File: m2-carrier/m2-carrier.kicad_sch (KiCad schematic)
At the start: 29 parts, among them P1 ESC1_VCC, P2 ESC1_GND, P3 LIPO_VCC, P4 LIPO_GND, P5 ESC2_VCC, P6 ESC2_GND, Q1 DMP3013SFV, U2 LD1117S33TR_SOT223, U6 LMR16030SDDAR

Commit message: new stuff
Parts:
- removed C21, C23: 2.2uF, Capacitor_SMD:C_0402_1005Metric, symbol Device:C_Small
- removed C24, C27: 47uF, Capacitor_SMD:C_0402_1005Metric, symbol Device:C_Small
- removed C28, C29, C32: 100nF, Capacitor_SMD:C_0402_1005Metric, symbol Device:C_Small
- removed C3, C5: 10uF, Capacitor_SMD:C_0402_1005Metric_Pad0.74x0.62mm_HandSolder, symbol Device:C_Small
- removed C30: 10uF, Capacitor_SMD:C_0402_1005Metric, symbol Device:C_Small
- removed C31: C_SS, Capacitor_SMD:C_0402_1005Metric, symbol Device:C_Small
- removed D7: B340AG, Diode_SMD:D_SMB, symbol Device:D_Schottky_Small
- removed D8: MMBZ5242B, Diode_SMD:D_SOT-23_ANK, symbol Diode:BZV55C12
- removed JP1: SolderJumper_3_Open, Jumper:SolderJumper-3_P1.3mm_Open_RoundedPad1.0x1.5mm_NumberLabels, symbol Jumper:SolderJumper_3_Open
- removed JP3: IO_EN, Jumper:SolderJumper-2_P1.3mm_Open_RoundedPad1.0x1.5mm, symbol Jumper:SolderJumper_2_Open
- removed L2: 8.2uH, Inductor_SMD:L_Bourns_SRP7028A_7.3x6.6mm, symbol Device:L_Small
- removed P1: ESC1_VCC, TestPoint:TestPoint_Pad_2.0x2.0mm, symbol hermes_v1-rescue:PAD_SMD-pkl_misc
- removed P2: ESC1_GND, TestPoint:TestPoint_Pad_D2.0mm, symbol hermes_v1-rescue:PAD_SMD-pkl_misc
- removed P3: LIPO_VCC, TestPoint:TestPoint_Pad_2.0x2.0mm, symbol hermes_v1-rescue:PAD_SMD-pkl_misc
- removed P4: LIPO_GND, TestPoint:TestPoint_Pad_D2.0mm, symbol hermes_v1-rescue:PAD_SMD-pkl_misc
- removed P5: ESC2_VCC, TestPoint:TestPoint_Pad_2.0x2.0mm, symbol hermes_v1-rescue:PAD_SMD-pkl_misc
- removed P6: ESC2_GND, TestPoint:TestPoint_Pad_D2.0mm, symbol hermes_v1-rescue:PAD_SMD-pkl_misc
- removed Q1: DMP3013SFV, Package_SON:Diodes_PowerDI3333-8, symbol Transistor_FET:DMP3013SFV
- removed R10: 49.9K, Resistor_SMD:R_0402_1005Metric, symbol Device:R_Small
- removed R11: 17.8K, Resistor_SMD:R_0402_1005Metric, symbol Device:R_Small
- removed R17: 12K, Resistor_SMD:R_0402_1005Metric, symbol Device:R_Small
- removed R8: 100K, Resistor_SMD:R_0402_1005Metric, symbol Device:R_Small
- removed U2: LD1117S33TR_SOT223, Package_TO_SOT_SMD:SOT-223-3_TabPin2, symbol Regulator_Linear:LD1117S33TR_SOT223
- removed U6: LMR16030SDDAR, Package_SO:Texas_HSOP-8-1EP_3.9x4.9mm_P1.27mm_ThermalVias, symbol Regulator_Switching:LMR33630ADDA
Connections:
- no-connect marks 1 -> 0
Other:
- removed sheet PADS
- note removed: "+5V @ 3A DC-DC Converter (4.3v-60v Input)"
- note removed: "2.1mm Tip +12v input Voltage"
- note removed: "3A RMS Current 6A I_Saturation"
- note removed: "By default, the usb port are connected to the 3.3V LDO If bridged, LDO receives power from buck regulator"
- note removed: "C_BOOT"
- note removed: "C_SS"
- note removed: "Diode to prevent reverse polarity at input"
- note removed: "ESC Solder Pads"
- note removed: "LiPo Battery Solder Pads"
- note removed: "Linear Dropout Regulator - LD1117 - 3.3V 1A"
- note removed: "Maximum input voltage: 26V"
- note removed: "Power"
- note removed: "R_FBB"
- note removed: "R_FBT"
- note removed: "Rated for 16V"
- note removed: "SOT23-3 225mW-300mW"
- note removed: "Solder-Jumper for USB_VBUS and 5V"

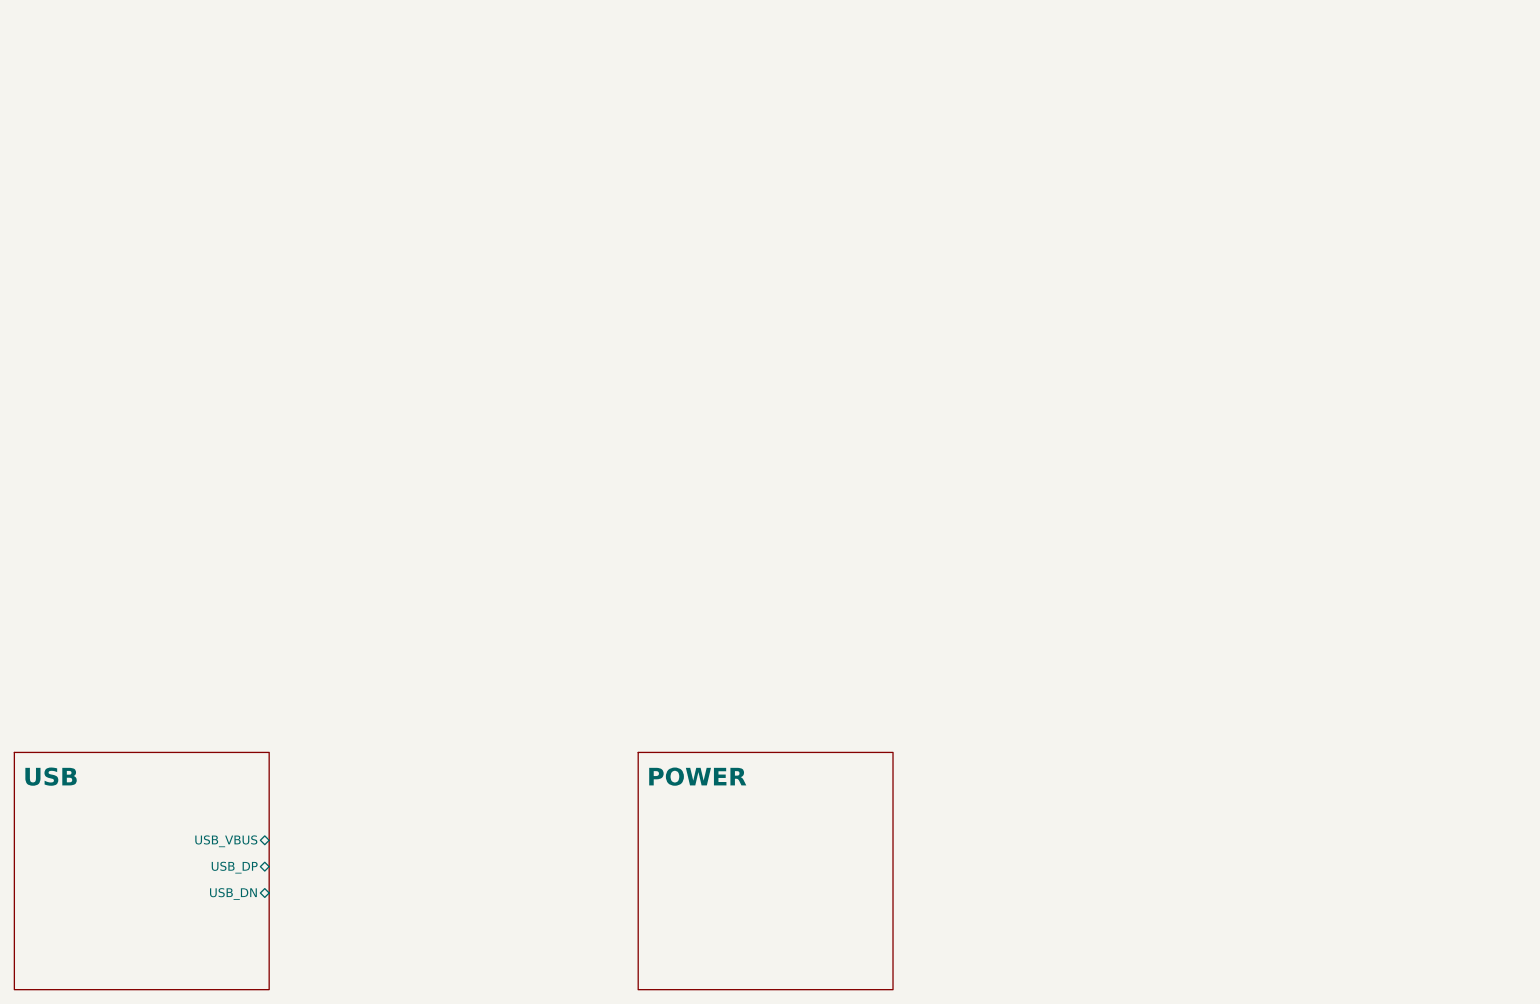
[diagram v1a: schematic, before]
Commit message: added video IC
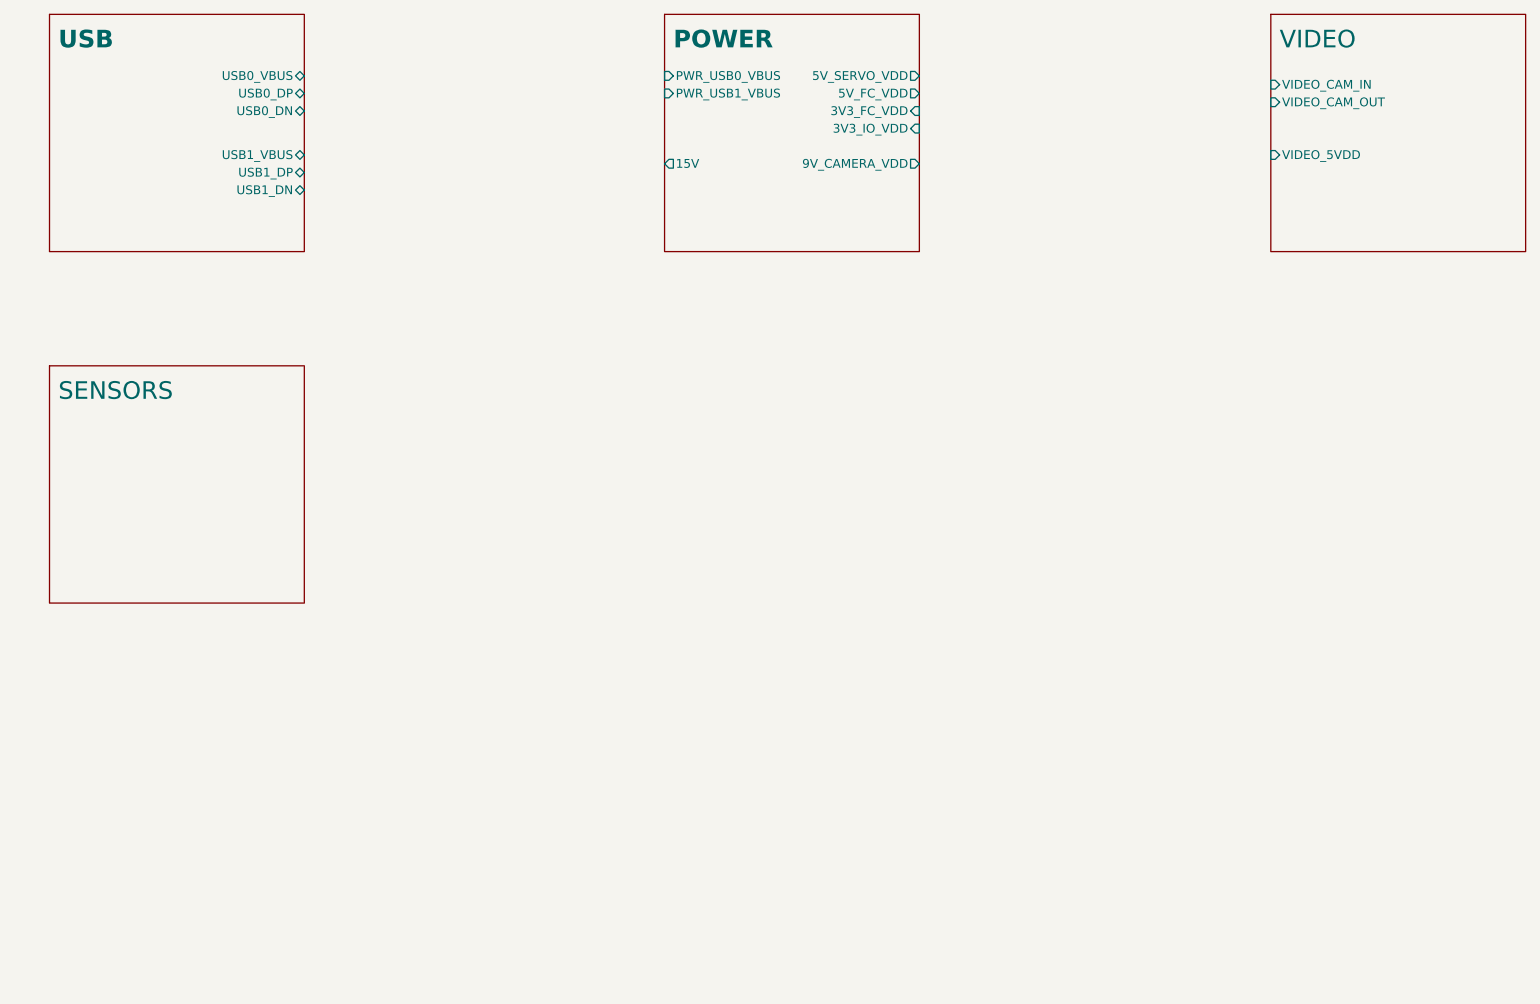
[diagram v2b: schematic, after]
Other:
- added sheet SENSORS (SENSORS.kicad_sch)
- added sheet VIDEO (VIDEO.kicad_sch)
- sheet POWER ports: added 15V, 3V3_FC_VDD, 3V3_IO_VDD, 5V_FC_VDD, 5V_SERVO_VDD, 9V_CAMERA_VDD, PWR_USB0_VBUS, PWR_USB1_VBUS; removed none
- sheet USB ports: added USB0_DN, USB0_DP, USB0_VBUS, USB1_DN, USB1_DP, USB1_VBUS; removed USB_DN, USB_DP, USB_VBUS
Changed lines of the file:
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@@
 (kicad_sch (version 20230121) (generator eeschema)
   (paper "A4")
-  (sheet (at 27.94 142.24) (size 36.83 34.29)
+  (sheet (at 209.55 35.56) (size 36.83 34.29)
+    (stroke (width 0.1524) (type solid))
+    (fill (color 194 194 194 1.0000))
+    (property "Sheetname" "VIDEO" (at 210.82 40.64 0)
+      (effects (font (face "Fira Code Retina") (size 2.54 2.54)) (justify left bottom))
+    )
+    (property "Sheetfile" "VIDEO.kicad_sch" (at 209.55 67.8946 0)
+      (effects (font (size 1.27 1.27)) (justify left top) hide)
+    )
+    (pin "VIDEO_CAM_IN" input (at 209.55 45.72 180)
+      (effects (font (size 1.27 1.27)) (justify left))
+    )
+    (pin "VIDEO_CAM_OUT" input (at 209.55 48.26 180)
+      (effects (font (size 1.27 1.27)) (justify left))
+    )
+    (pin "VIDEO_5VDD" input (at 209.55 55.88 180)
+      (effects (font (size 1.27 1.27)) (justify left))
+    )
+    (instances
+      (project "m2-carrier"
+        (path "/5f2bc0b3-3222-4ac4-baca-7f43b47f8a71" (page "4"))
+      )
+    )
+  )
+  (sheet (at 33.02 35.56) (size 36.83 34.29)
     (stroke (width 0.1524) (type solid))
     (fill (color 255 255 194 1.0000))
-    (property "Sheetname" "USB" (at 29.21 147.32 0)
+    (property "Sheetname" "USB" (at 34.29 40.64 0)
       (effects (font (face "Fira Code Retina") (size 2.54 2.54) bold) (justify left bottom))
     )
-    (property "Sheetfile" "USB.kicad_sch" (at 27.94 173.99 0)
+    (property "Sheetfile" "USB.kicad_sch" (at 33.02 67.31 0)
       (effects (font (size 1.27 1.27)) (justify left top) hide)
     )
-    (pin "USB_VBUS" bidirectional (at 64.77 154.94 0)
+    (pin "USB0_VBUS" bidirectional (at 69.85 44.45 0)
       (effects (font (size 1.27 1.27)) (justify right))
     )
-    (pin "USB_DP" bidirectional (at 64.77 158.75 0)
+    (pin "USB0_DP" bidirectional (at 69.85 46.99 0)
       (effects (font (size 1.27 1.27)) (justify right))
     )
-    (pin "USB_DN" bidirectional (at 64.77 162.56 0)
+    (pin "USB0_DN" bidirectional (at 69.85 49.53 0)
+      (effects (font (size 1.27 1.27)) (justify right))
+    )
+    (pin "USB1_VBUS" bidirectional (at 69.85 55.88 0)
+      (effects (font (size 1.27 1.27)) (justify right))
+    )
+    (pin "USB1_DP" bidirectional (at 69.85 58.42 0)
+      (effects (font (size 1.27 1.27)) (justify right))
+    )
+    (pin "USB1_DN" bidirectional (at 69.85 60.96 0)
       (effects (font (size 1.27 1.27)) (justify right))
     )
@@
     )
   )
-  (sheet (at 118.11 142.24) (size 36.83 34.29)
+  (sheet (at 121.92 35.56) (size 36.83 34.29)
     (stroke (width 0.1524) (type solid))
     (fill (color 255 229 191 1.0000))
-    (property "Sheetname" "POWER" (at 119.38 147.32 0)
+    (property "Sheetname" "POWER" (at 123.19 40.64 0)
       (effects (font (face "Fira Code Retina") (size 2.54 2.54) bold) (justify left bottom))
     )
-    (property "Sheetfile" "POWER.kicad_sch" (at 118.11 173.99 0)
+    (property "Sheetfile" "POWER.kicad_sch" (at 121.92 67.31 0)
       (effects (font (size 1.27 1.27)) (justify left top) hide)
+    )
+    (pin "5V_SERVO_VDD" output (at 158.75 44.45 0)
+      (effects (font (size 1.27 1.27)) (justify right))
+    )
+    (pin "5V_FC_VDD" output (at 158.75 46.99 0)
+      (effects (font (size 1.27 1.27)) (justify right))
+    )
+    (pin "9V_CAMERA_VDD" output (at 158.75 57.15 0)
+      (effects (font (size 1.27 1.27)) (justify right))
+    )
+    (pin "15V" output (at 121.92 57.15 180)
+      (effects (font (size 1.27 1.27)) (justify left))
+    )
+    (pin "3V3_FC_VDD" input (at 158.75 49.53 0)
+      (effects (font (size 1.27 1.27)) (justify right))
+    )
+    (pin "3V3_IO_VDD" input (at 158.75 52.07 0)
+      (effects (font (size 1.27 1.27)) (justify right))
+    )
+    (pin "PWR_USB1_VBUS" input (at 121.92 46.99 180)
+      (effects (font (size 1.27 1.27)) (justify left))
+    )
+    (pin "PWR_USB0_VBUS" input (at 121.92 44.45 180)
+      (effects (font (size 1.27 1.27)) (justify left))
     )
     (instances
@@
       )
     )
+  )
+  (sheet (at 33.02 86.36) (size 36.83 34.29)
+    (stroke (width 0.1524) (type solid))
+    (fill (color 0 0 0 0.0000))
+    (property "Sheetname" "SENSORS" (at 34.29 91.44 0)
+      (effects (font (face "Fira Code Retina") (size 2.54 2.54)) (justify left bottom))
+    )
+    (property "Sheetfile" "SENSORS.kicad_sch" (at 33.02 118.6946 0)
+      (effects (font (size 1.27 1.27)) (justify left top) hide)
+    )
+    (instances
+      (project "m2-carrier"
+        (path "/5f2bc0b3-3222-4ac4-baca-7f43b47f8a71" (page "5"))
+      )
+    )

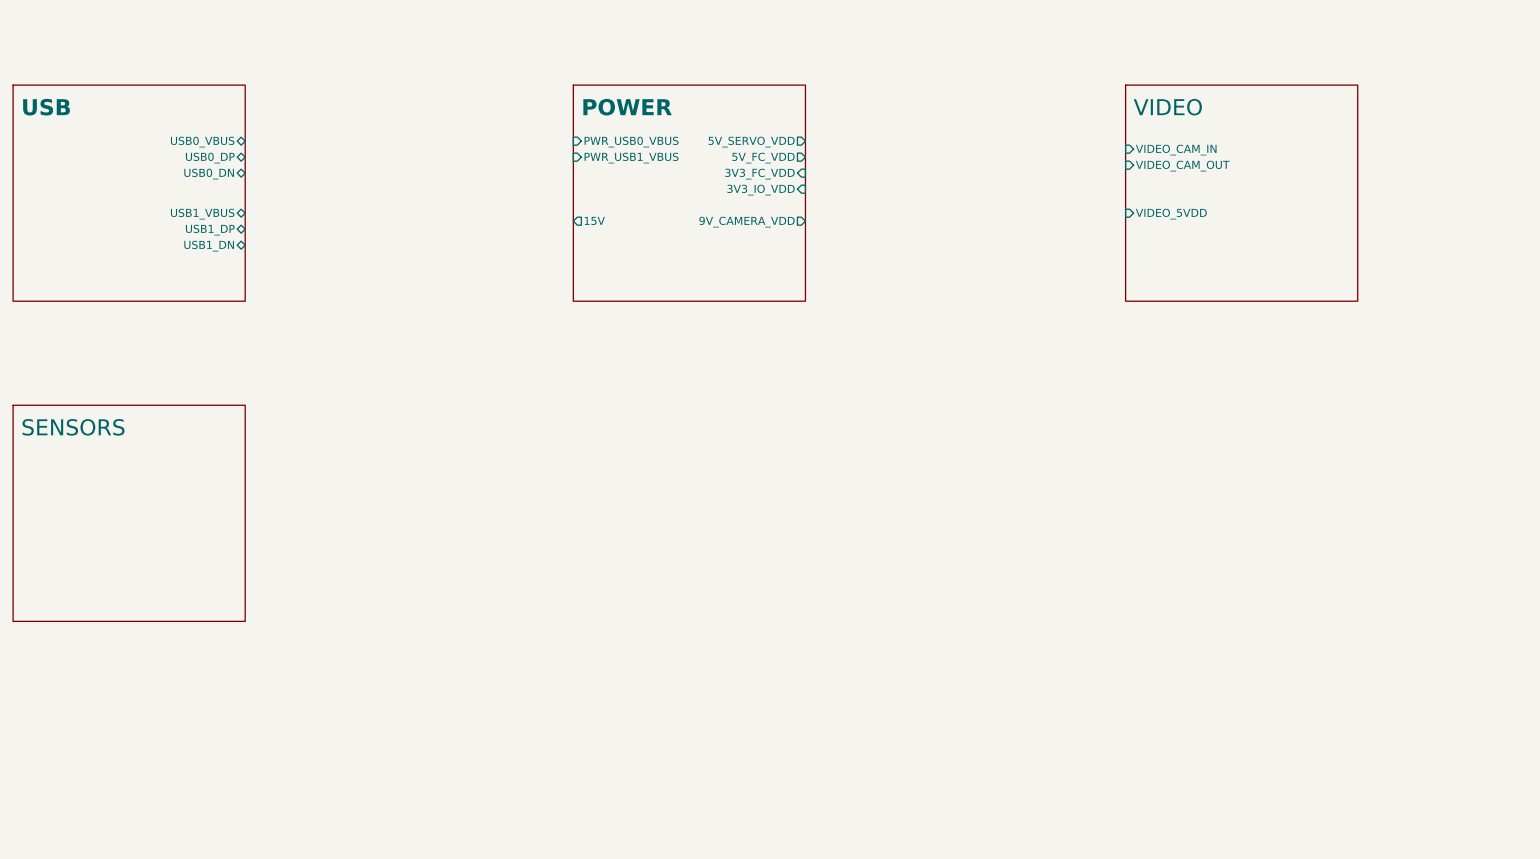
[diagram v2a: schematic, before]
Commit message: Added base board
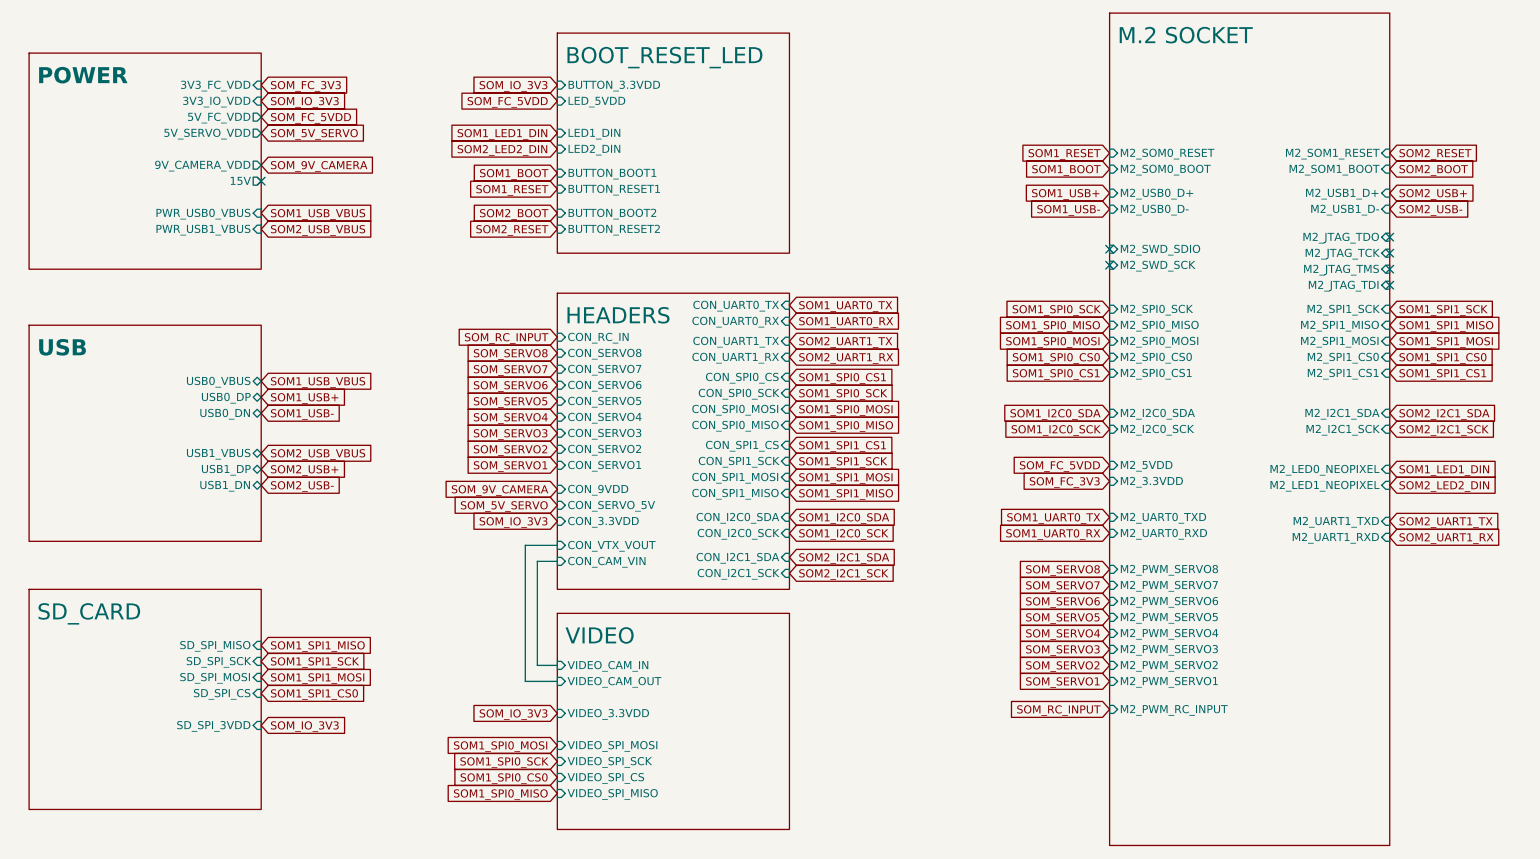
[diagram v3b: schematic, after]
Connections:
- no-connect marks 0 -> 7
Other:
- removed sheet SENSORS
- added sheet BOOT_RESET_LED (BOOT_RESET_LED.kicad_sch)
- added sheet HEADERS (PIN_HEADER.kicad_sch)
- added sheet M.2 SOCKET (M2_SOCKET.kicad_sch)
- added sheet SD_CARD (SD_CARD.kicad_sch)
- sheet VIDEO ports: added VIDEO_3.3VDD, VIDEO_SPI_CS, VIDEO_SPI_MISO, VIDEO_SPI_MOSI, VIDEO_SPI_SCK; removed VIDEO_5VDD
